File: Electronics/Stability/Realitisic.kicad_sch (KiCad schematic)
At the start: 6 parts, among them U2 ${SIM.PARAMS}

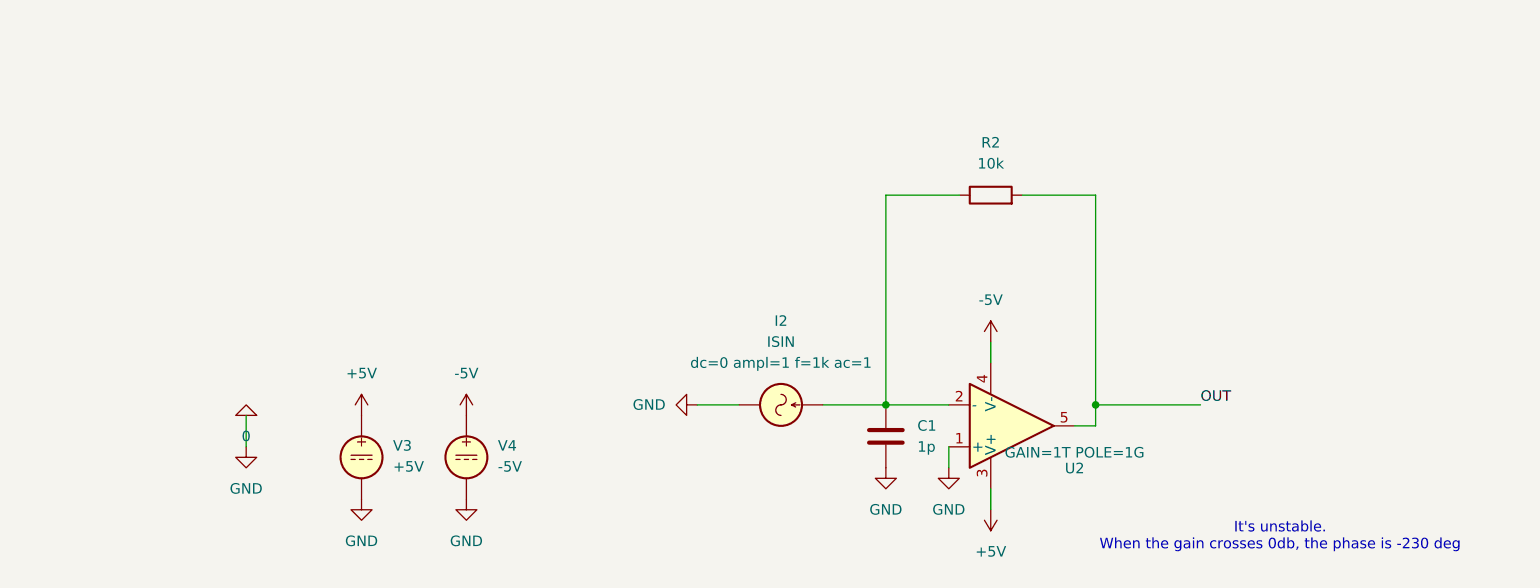
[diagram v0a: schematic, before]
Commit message: Add OPA858 stability simulation
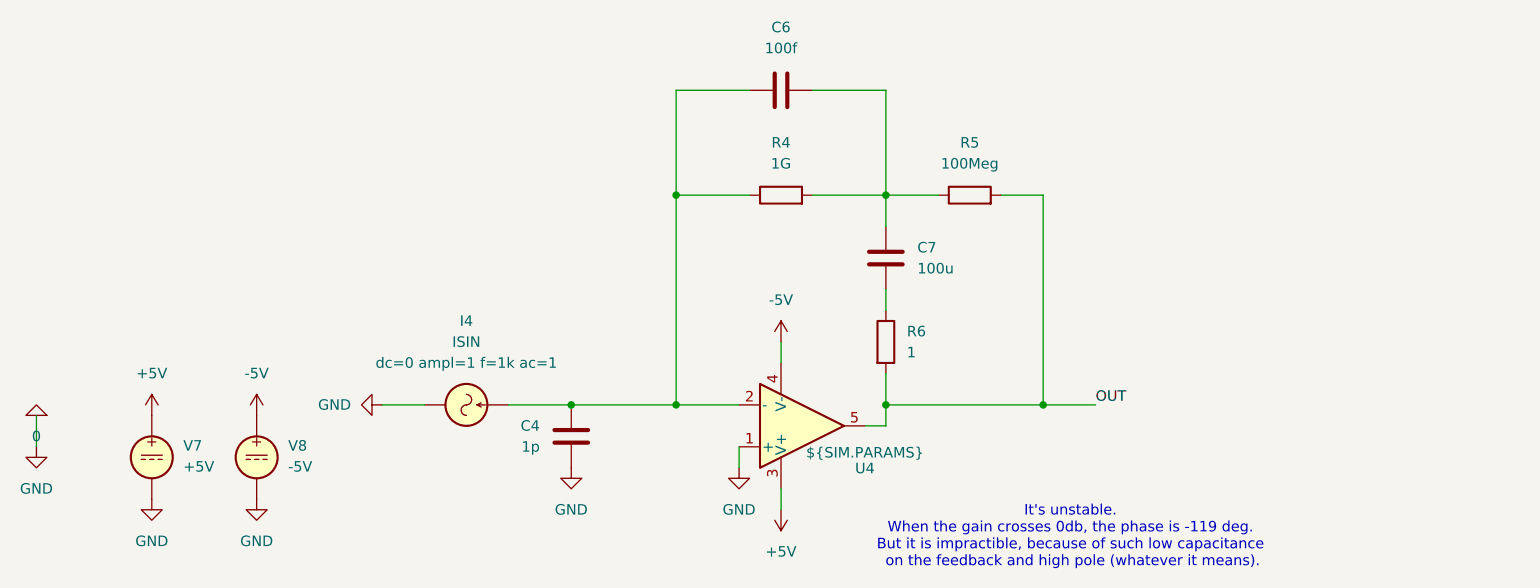
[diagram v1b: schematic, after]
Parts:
- removed C1: 1p, symbol Device:C
- removed I2: ISIN, symbol Simulation_SPICE:ISIN
- removed R2: 10k, symbol Device:R
- removed U2: ${SIM.PARAMS}, symbol Simulation_SPICE:OPAMP
- removed V3: +5V, symbol Simulation_SPICE:VDC
- removed V4: -5V, symbol Simulation_SPICE:VDC
- added C4: 1p, symbol Device:C
- added C6: 100f, symbol Device:C
- added C7: 100u, symbol Device:C
- added I4: ISIN, symbol Simulation_SPICE:ISIN
- added R4: 1G, symbol Device:R
- added R5: 100Meg, symbol Device:R
- added R6: 1, symbol Device:R
- added U4: ${SIM.PARAMS}, symbol Simulation_SPICE:OPAMP
- added V7: +5V, symbol Simulation_SPICE:VDC
- added V8: -5V, symbol Simulation_SPICE:VDC
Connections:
- net +5V: now also U4.3 (V+), V7.1
- net -5V: now also U4.4 (V-), V8.1
- net 0: now also C4.2, I4.2, U4.1 (+), V7.2, V8.2
- net OUT: now also R5.2, R6.2, U4.5
- new net: C4.1, C6.1, I4.1, R4.1, U4.2 (-)
- new net: C6.2, C7.2, R4.2, R5.1
- new net: C7.1, R6.1
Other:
- note added: "It's unstable. When the gain crosses 0db, the phase is -119 deg. But it is impractible, because of such low capacitance on the feedback and high pole (whatever it means)."
- note removed: "It's unstable. When the gain crosses 0db, the phase is -230 deg"
